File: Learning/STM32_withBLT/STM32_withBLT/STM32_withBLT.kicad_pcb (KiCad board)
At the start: 4 copper layers, 62.2 x 27.3 mm, 51 parts, among them J1 Conn_01x04, J2 Conn_Coaxial, J3 USB_C_Receptacle_USB2.0_16P, J4 Conn_01x10, SW1 SW_Push, U1 MIC5365-3.3YD5, U2 USBLC6-2SC6, U3 STM32WB55CEU6, X1 32kHz768, X2 32MHz

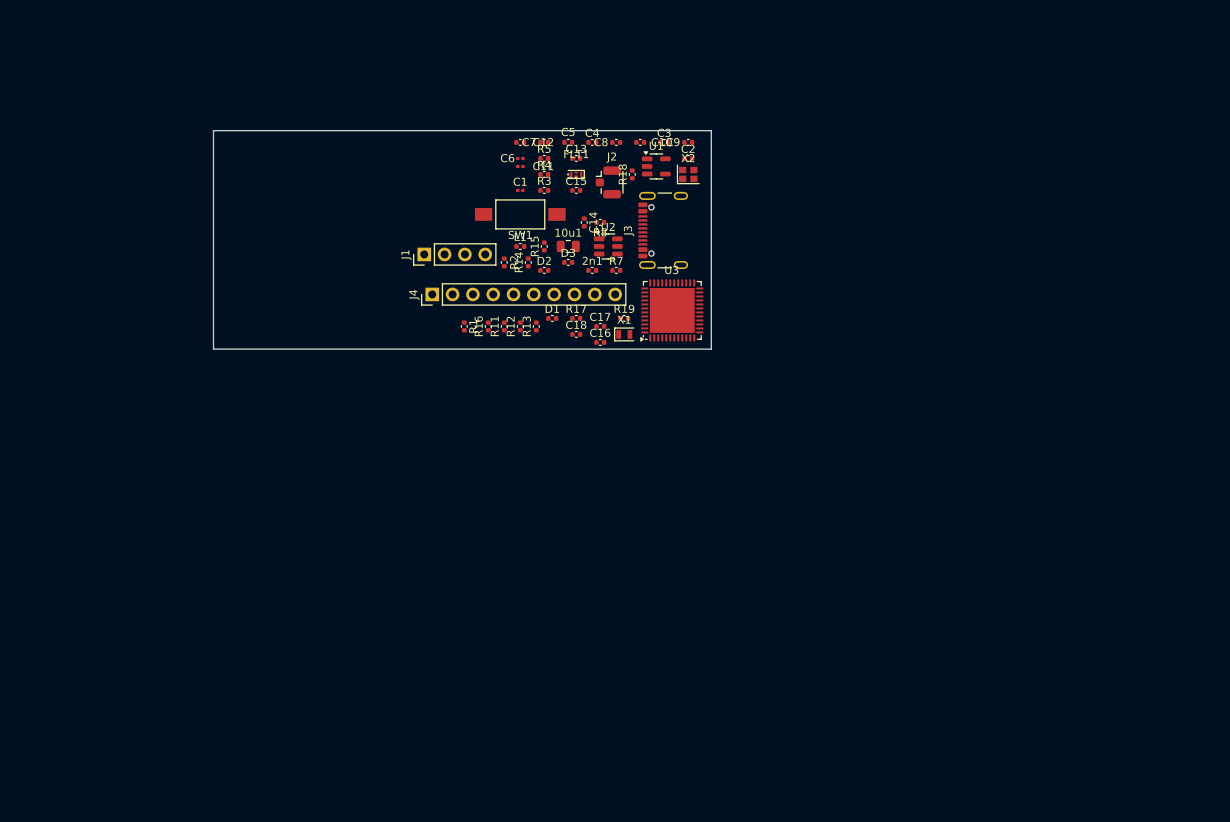
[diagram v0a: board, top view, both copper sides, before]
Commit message: stm32 initial pcb layoout
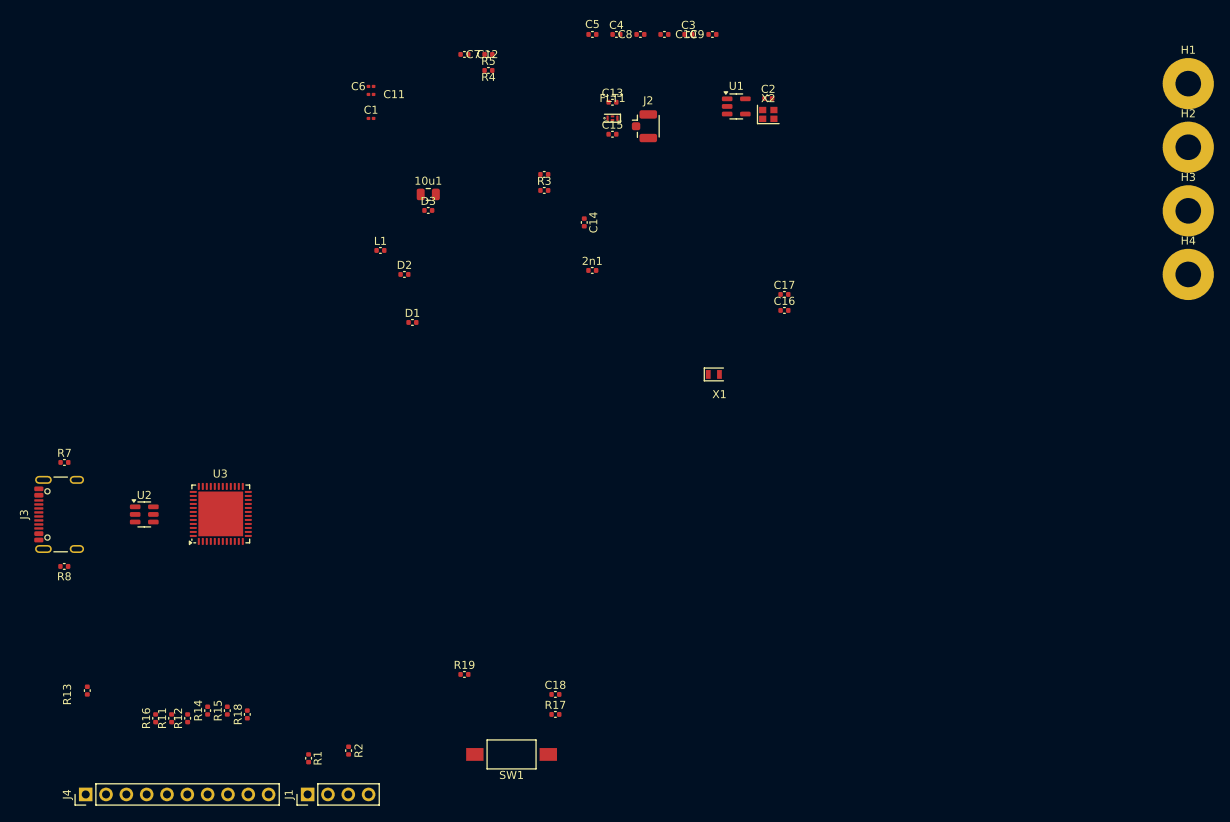
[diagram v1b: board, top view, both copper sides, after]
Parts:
- added H1: MountingHole, MountingHole:MountingHole_3.2mm_M3_Pad, F.Cu at (242.5, 43.6)
- added H2: MountingHole, MountingHole:MountingHole_3.2mm_M3_Pad, F.Cu at (242.5, 51.6)
- added H3: MountingHole, MountingHole:MountingHole_3.2mm_M3_Pad, F.Cu at (242.5, 59.5)
- added H4: MountingHole, MountingHole:MountingHole_3.2mm_M3_Pad, F.Cu at (242.5, 67.5)
- moved J3 83.4 mm to (102.5, 97.5)
- moved R18 82.9 mm to (124.9, 122.5)
- moved R8 79.6 mm to (102.0, 104.0)
- moved J4 76.0 mm to (104.7, 132.5)
- moved R7 73.0 mm to (102.0, 91.0)
- moved R13 72.3 mm to (104.9, 119.5)
- moved R15 70.3 mm to (122.4, 122.0)
- moved J1 69.1 mm to (132.4, 132.5)
- moved R14 68.9 mm to (119.9, 122.0)
- moved SW1 67.5 mm to (157.9, 127.5)
- moved U2 67.0 mm to (112.0, 97.5)
- moved R11 64.2 mm to (115.4, 123.0)
- moved R12 64.2 mm to (117.4, 123.0)
- moved R16 64.2 mm to (113.4, 123.0)
- moved R2 64.0 mm to (137.5, 127.0)
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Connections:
- net Net-(R17-Pad2) renamed /BOOT_SW_OUT
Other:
- board outline removed

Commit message: test
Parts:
- moved C2 5.88 mm to (195.9, 46.0)
- moved U1 5.88 mm to (191.9, 47.0)
- moved X2 5.88 mm to (195.9, 48.0)
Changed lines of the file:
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@@
 		(placed yes)
 		(layer "F.Cu")
-		(at 190 45.5)
+		(at 195.8625 45.95)
 		(descr "Capacitor SMD 0402 (1005 Metric), square (rectangular) end terminal, IPC_7351 nominal, (Body size source: IPC-SM-782 page 76, https://www.pcb-3d.com/wordpress/wp-content/uploads/ipc-sm-782a_amendment_1_and_2.pdf), generated with kicad-footprint-generator")
 		(tags "capacitor")
@@
 		(placed yes)
 		(layer "F.Cu")
-		(at 190 47.5)
+		(at 195.8625 47.95)
 		(descr "SMD Crystal SERIES SMD2016/4 http://www.q-crystal.com/upload/5/2015552223166229.pdf, 2.0x1.6mm^2 package")
 		(tags "SMD SMT crystal")
@@
 		(placed yes)
 		(layer "F.Cu")
-		(at 186 46.5)
+		(at 191.8625 46.95)
 		(descr "SOT, 5 Pin (JEDEC MO-178 Var AA https://www.jedec.org/document_search?search_api_views_fulltext=MO-178), generated with kicad-footprint-generator ipc_gullwing_generator.py")
 		(tags "SOT TO_SOT_SMD")
